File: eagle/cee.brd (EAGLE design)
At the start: 50 x 80 mm, 52 parts, among them IC1 IC1, J1 SOLDERJUMPERNC2

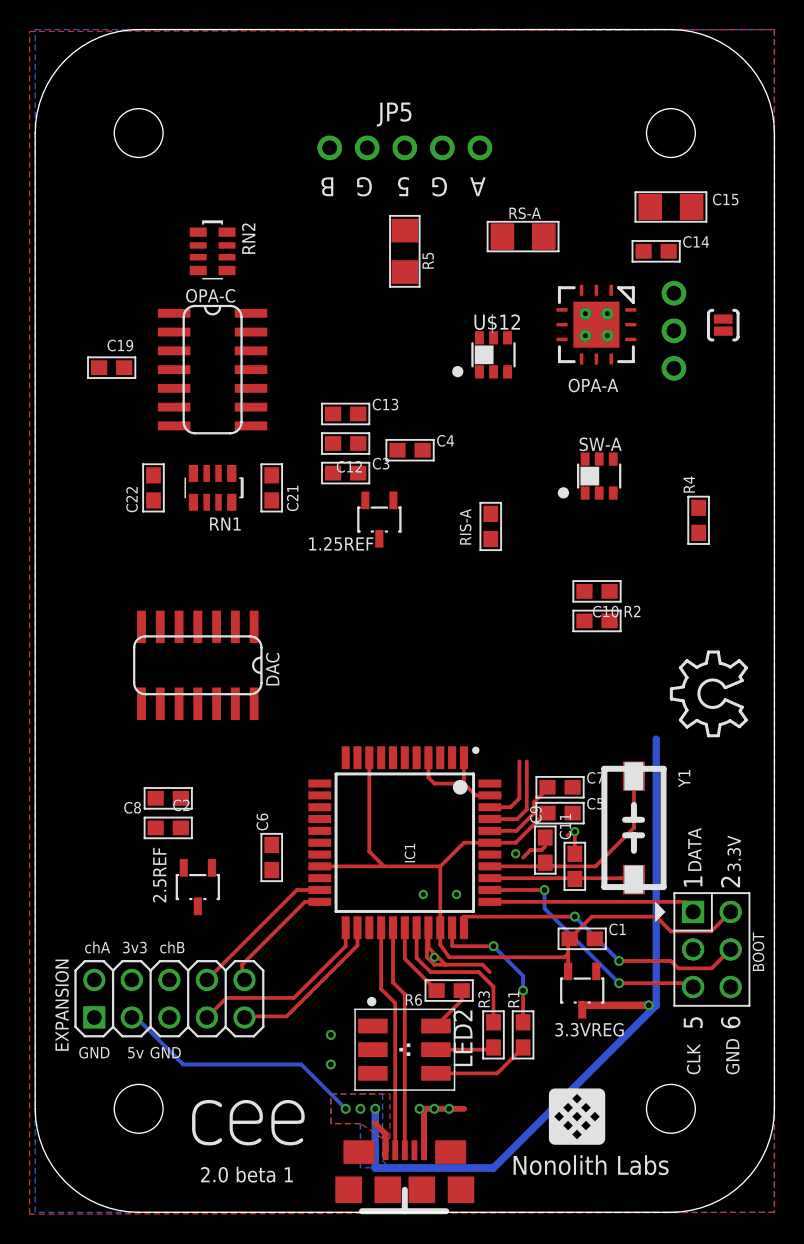
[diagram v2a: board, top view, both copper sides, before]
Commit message: more routing, moved some stuff around
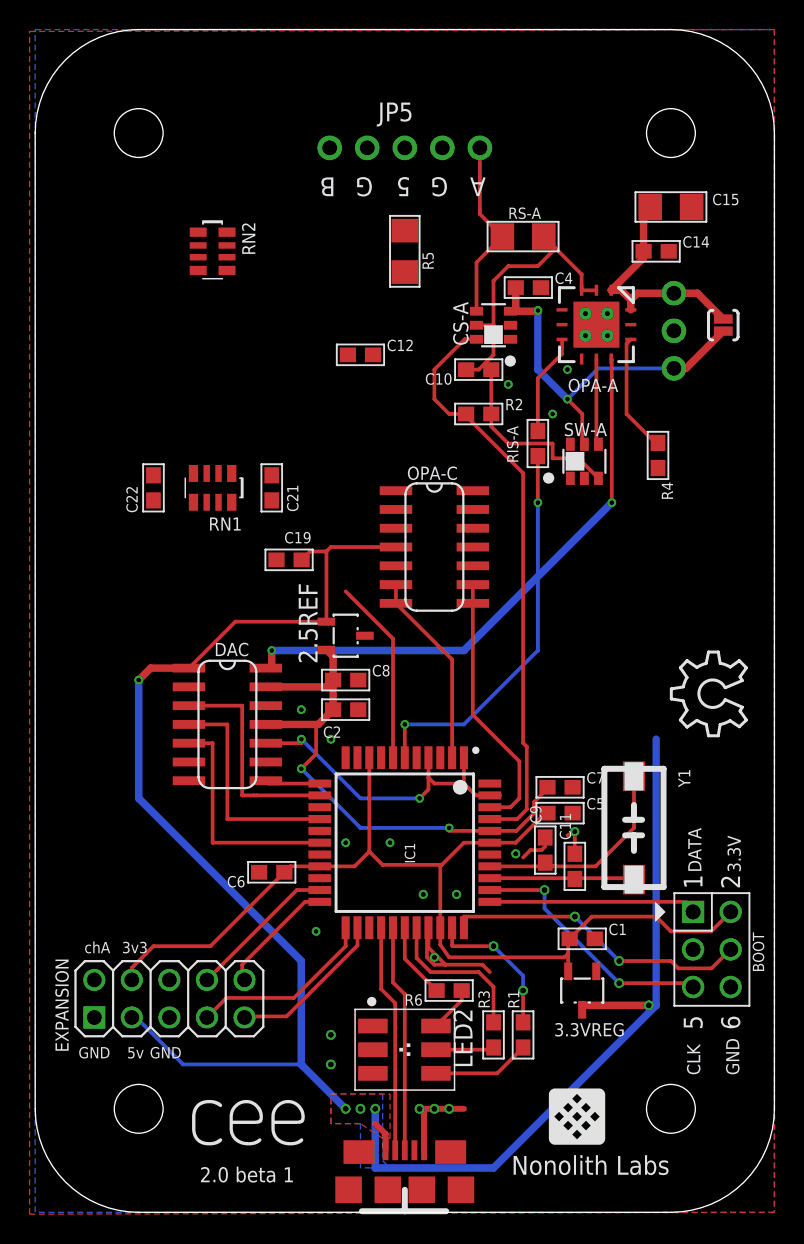
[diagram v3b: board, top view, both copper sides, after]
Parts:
- removed 1.25REF: (no value), nonolith:SOT23-3
- removed C13, C3: .01uF, nonolith:0603
- removed U$12: INA213, nonolith:SOT23-6
- added CS-A: INA213, nonolith:SOT23-6
- C12: value 1uF -> .01uF
- OPA-C: value AD86080.0254 -> AD8608
- moved 2.5REF 19.7 mm to (21.0, 39.0), turned to 90 degrees
- moved OPA-C 19.2 mm to (27.0, 45.0)
- moved C19 17.7 mm to (17.2, 44.1)
- moved C10 17.0 mm to (30.0, 57.0)
- moved R2 16.1 mm to (30.0, 54.0)
- moved C2 14.4 mm to (21.0, 34.0), turned to 0 degrees
- moved C8 14.4 mm to (21.0, 36.0), turned to 0 degrees
- moved C4 13.6 mm to (33.4, 62.5)
- moved RIS-A 6.45 mm to (34.0, 52.0)
- moved C12 6.08 mm to (22.0, 58.0)
- moved R4 5.18 mm to (42.1, 51.2), turned to 270 degrees
- moved DAC 4.47 mm to (13.0, 33.0), turned to 270 degrees
- moved SW-A 1.41 mm to (37.1, 50.8)
- moved C6 1.00 mm to (16.0, 23.0), turned to 180 degrees
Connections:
- removed net 1.25VREF: 1.25REF.2, C12.1, C13.1, C3.1, IC1.1, IC1.4, IC1.43, U$12.1
- removed net N$13: JP5.5
- removed net SMU-B: EXPANSION.6, RN2.3
- new net CSA-VREF: C12.1, CS-A.1, IC1.7
- net 5V: now also CS-A.3; no longer 1.25REF.1, U$12.3
- net GND: now also CS-A.2; no longer 1.25REF.3, C13.2, C3.2, U$12.2
- net SMU-A: now also CS-A.4; no longer U$12.4
- net VO-A: now also CS-A.5; no longer U$12.5
- net VOUT-B: now also IC1.1, IC1.4, IC1.43
- net VS-A: now also CS-A.6; no longer U$12.6
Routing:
- net 5V: track 70.0 -> 153.0 mm, vias 4 -> 7
- net VOUT-A: track 0.00 -> 38.5 mm, vias 0 -> 2
- net VS-A: track 6.02 -> 39.5 mm
- net 2.5VREF: track 5.66 -> 39.1 mm, vias 0 -> 2
- net ISET-DAC-A: track 0.00 -> 26.5 mm, vias 0 -> 2
- net VOUT-B: track 0.00 -> 22.4 mm, vias 0 -> 2
- net VO-A: track 0.00 -> 19.2 mm
- net 5V-EXT: track 0.00 -> 16.2 mm
- net 3.3V: track 53.7 -> 69.7 mm
- net MOSI: track 0.00 -> 15.6 mm
- net SCK: track 0.00 -> 15.2 mm
- net CS: track 0.00 -> 14.9 mm
- net AF-A: track 0.00 -> 13.4 mm
- net ADC-B: track 0.00 -> 13.3 mm
- net ADC-A: track 4.75 -> 18.0 mm
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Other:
- board text removed: "chB"

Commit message: did I winzorz
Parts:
- added C13: .1uF, nonolith:0603
- added C16: (no value), nonolith:0603
- added C3: 4.7uF, nonolith:0603
- added U$12: LME49726, nonolith:SO-08
- CS-A: device nonolith:SOT23-6 -> nonolith:SC-70
- moved RN2 13.9 mm to (24.0, 58.0), turned to 180 degrees
- moved C12 10.9 mm to (32.8, 56.2), turned to 270 degrees
- moved C10 1.00 mm to (29.0, 57.0), turned to 90 degrees
- moved R5 1.00 mm to (26.0, 65.0)
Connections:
- removed net 5V-EXT-P: JP5.3, R5.2
- new net 2.5VFDBK: R5.1, U$12.1
- new net 2.5VOUT: JP5.3, R5.2, U$12.2
- new net 5VOUT: JP5.5, U$12.6, U$12.7
- net 2.5VREF: now also C16.1, U$12.3
- net 5V: now also C13.1, C3.1, CS-A.P3, U$12.5, U$12.8; no longer CS-A.3
- net 5V-EXT: no longer R5.1
- net CSA-VREF: now also CS-A.P1; no longer CS-A.1
- net GND: now also C13.2, C16.2, C3.2, CS-A.P2, U$12.4; no longer CS-A.2
- net SMU-A: now also CS-A.P4; no longer CS-A.4, EXPANSION.2
- net VO-A: now also CS-A.P5; no longer CS-A.5
- net VS-A: now also CS-A.P6; no longer CS-A.6
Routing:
- net 5V: track 153.0 -> 205.3 mm, vias 7 -> 8
- net 2.5VREF: track 39.1 -> 81.6 mm, vias 2 -> 4
- net CSA-VREF: track 12.6 -> 47.0 mm, vias 0 -> 4
- net N$1: track 0.00 -> 30.1 mm, vias 0 -> 2
- net 2.5VOUT: track 0.00 -> 22.0 mm, vias 0 -> 2
- net BUFF-A: track 0.00 -> 20.7 mm, vias 0 -> 2
- net N$2: track 0.00 -> 20.3 mm, vias 0 -> 2
- net BUFF-B: track 0.00 -> 18.6 mm
- net SMUP-A: track 0.00 -> 17.0 mm
- net SMUP-SW-A: track 0.00 -> 16.1 mm, vias 0 -> 2
- net 2.5VFDBK: track 0.00 -> 14.6 mm
- net SMUP-B: track 0.00 -> 12.9 mm
- net 5VOUT: track 0.00 -> 7.56 mm
- net SMU-A: track 12.4 -> 19.3 mm
- net VS-A: track 39.5 -> 41.3 mm
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
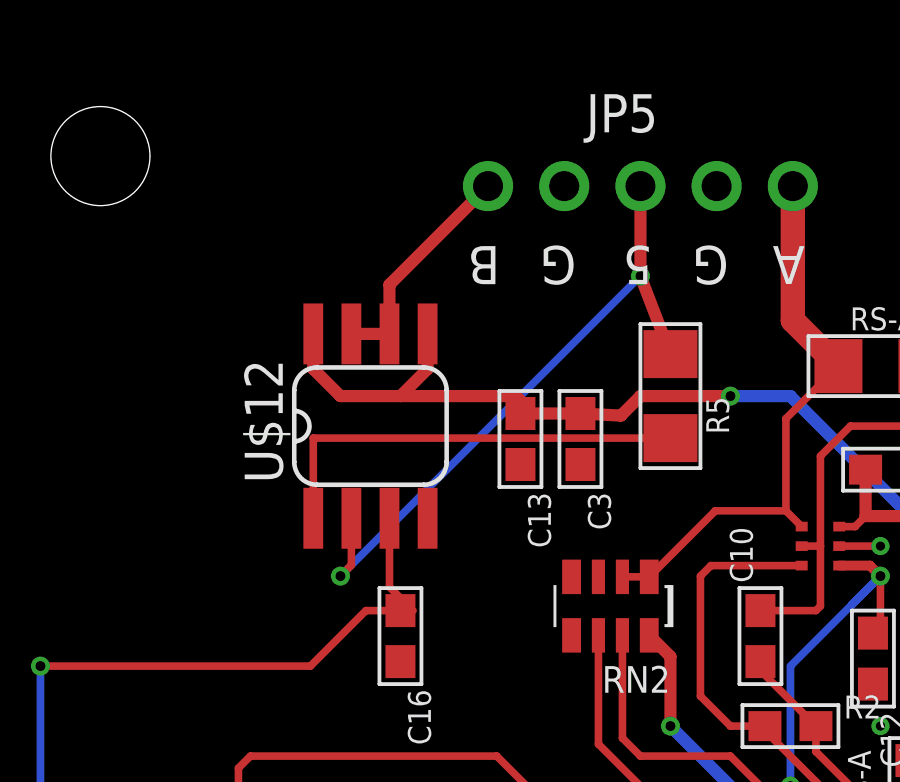
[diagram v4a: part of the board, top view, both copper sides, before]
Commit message: update package of buffer to correct layout
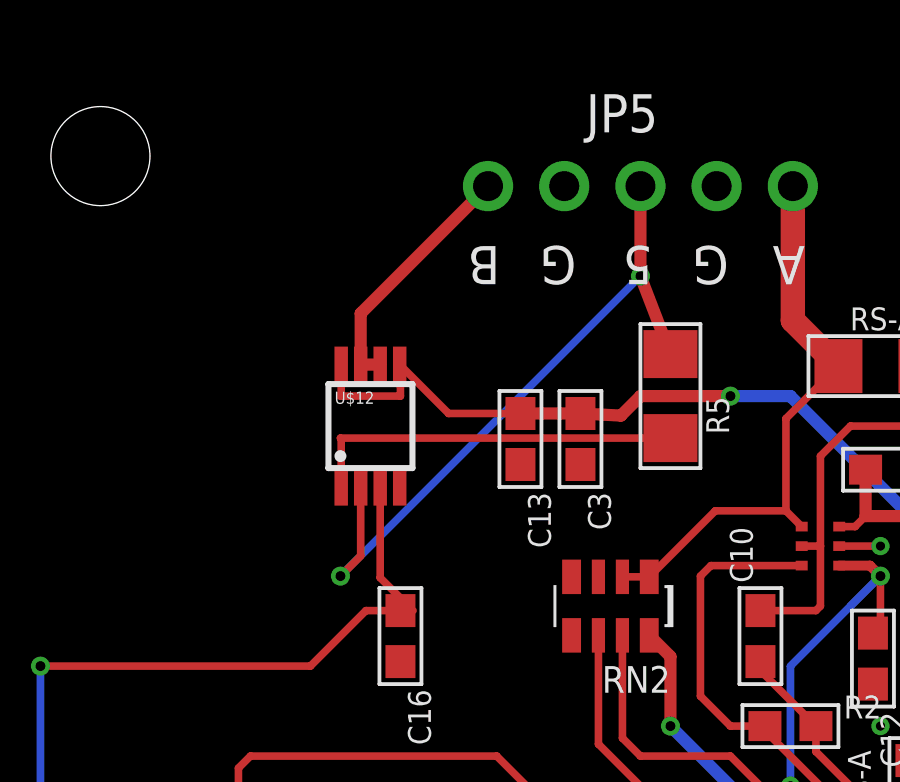
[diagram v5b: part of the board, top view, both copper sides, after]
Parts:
- U$12: device nonolith:SO-08 -> nonolith:MSOP8
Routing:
- net 5V: track 205.3 -> 202.6 mm
- net 2.5VFDBK: track 14.6 -> 12.7 mm
- net 2.5VREF: track 81.6 -> 82.8 mm
- net 2.5VOUT: track 22.0 -> 23.2 mm
- net 5VOUT: track 7.56 -> 8.36 mm
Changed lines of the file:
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@@
 <element name="CS-A" library="nonolith" package="SC-70" value="INA213" x="31" y="60" rot="R90"/>
 <element name="C12" library="nonolith" package="0603" value=".01uF" x="32.75" y="56.25" rot="R270"/>
-<element name="U$12" library="nonolith" package="SO-08" value="LME49726" x="16" y="64"/>
+<element name="U$12" library="nonolith" package="MSOP8" value="LME49726" x="16" y="64"/>
 <element name="C3" library="nonolith" package="0603" value="4.7uF" x="23" y="63.57" rot="R270"/>
 <element name="C13" library="nonolith" package="0603" value=".1uF" x="21" y="63.57" rot="R270"/>
@@
 <contactref element="C13" pad="1"/>
 <contactref element="C3" pad="1"/>
-<wire x1="18" y1="67.0734" x2="17.905" y2="67.0734" width="0.254" layer="1"/>
 <via x="28" y="65" extent="1-16" drill="0.3302"/>
 <wire x1="28" y1="65" x2="30" y2="65" width="0.4064" layer="16"/>
@@
 <wire x1="24.35" y1="64.35" x2="25" y2="65" width="0.4064" layer="1"/>
 <wire x1="25" y1="65" x2="28" y2="65" width="0.4064" layer="1"/>
-<wire x1="21" y1="64.42" x2="21" y2="64.85" width="0.4064" layer="1"/>
-<wire x1="14.095" y1="67.0734" x2="14.095" y2="65.905" width="0.4064" layer="1"/>
-<wire x1="14.095" y1="65.905" x2="15" y2="65" width="0.4064" layer="1"/>
-<wire x1="15" y1="65" x2="17" y2="65" width="0.4064" layer="1"/>
-<wire x1="17" y1="65" x2="17.905" y2="65.905" width="0.4064" layer="1"/>
-<wire x1="17.905" y1="65.905" x2="17.905" y2="67.0734" width="0.4064" layer="1"/>
-<wire x1="21" y1="64.85" x2="20.85" y2="65" width="0.4064" layer="1"/>
-<wire x1="20.85" y1="65" x2="17" y2="65" width="0.4064" layer="1"/>
+<wire x1="15.025" y1="66.05" x2="15.025" y2="65.025" width="0.254" layer="1"/>
+<wire x1="15.025" y1="65.025" x2="15" y2="65" width="0.254" layer="1"/>
+<wire x1="15" y1="65" x2="17" y2="65" width="0.254" layer="1"/>
+<wire x1="17" y1="65" x2="17" y2="66.025" width="0.254" layer="1"/>
+<wire x1="17" y1="66.025" x2="16.975" y2="66.05" width="0.254" layer="1"/>
+<wire x1="21" y1="64.42" x2="18.605" y2="64.42" width="0.254" layer="1"/>
+<wire x1="18.605" y1="64.42" x2="16.975" y2="66.05" width="0.254" layer="1"/>
 </signal>
 <signal name="GND">
@@
 <wire x1="22" y1="26" x2="28" y2="26" width="0.254" layer="16"/>
 <contactref element="U$12" pad="3"/>
-<wire x1="16.635" y1="60.9266" x2="16.635" y2="58.635" width="0.254" layer="1"/>
 <wire x1="14" y1="56" x2="5" y2="56" width="0.254" layer="1"/>
 <via x="5" y="56" extent="1-16" drill="0.3302"/>
@@
 <wire x1="14" y1="56" x2="15.85" y2="57.85" width="0.254" layer="1"/>
 <wire x1="15.85" y1="57.85" x2="17" y2="57.85" width="0.254" layer="1"/>
-<wire x1="16.635" y1="58.635" x2="17" y2="58.27" width="0.254" layer="1"/>
+<wire x1="16.325" y1="58.945" x2="17" y2="58.27" width="0.254" layer="1"/>
 <wire x1="17" y1="58.27" x2="17" y2="57.85" width="0.254" layer="1"/>
+<wire x1="16.325" y1="61.95" x2="16.325" y2="58.945" width="0.254" layer="1"/>
 <wire x1="34.75" y1="28.75" x2="34.65" y2="28.75" width="0" layer="19" extent="1-1"/>
 </signal>
@@
 <contactref element="U$12" pad="7"/>
 <contactref element="U$12" pad="6"/>
-<wire x1="16.635" y1="67.0734" x2="15.365" y2="67.0734" width="0.4064" layer="1"/>
-<wire x1="16.635" y1="67.0734" x2="16.635" y2="68.715" width="0.4064" layer="1"/>
-<wire x1="16.635" y1="68.715" x2="19.92" y2="72" width="0.4064" layer="1"/>
+<wire x1="16.325" y1="66.05" x2="15.675" y2="66.05" width="0.4064" layer="1"/>
+<wire x1="15.675" y1="67.755" x2="19.92" y2="72" width="0.4064" layer="1"/>
+<wire x1="15.675" y1="67.755" x2="15.675" y2="66.05" width="0.4064" layer="1"/>
 </signal>
 <signal name="2.5VOUT">
@@
 <wire x1="25" y1="69" x2="26" y2="66.4" width="0.4064" layer="1"/>
 <wire x1="25" y1="72" x2="25" y2="69" width="0.4064" layer="1"/>
-<wire x1="15.365" y1="60.9266" x2="15.365" y2="59.365" width="0.254" layer="1"/>
-<wire x1="15.365" y1="59.365" x2="15" y2="59" width="0.254" layer="1"/>
+<wire x1="15.675" y1="59.675" x2="15" y2="59" width="0.254" layer="1"/>
 <via x="15" y="59" extent="1-16" drill="0.3302"/>
 <wire x1="15" y1="59" x2="25" y2="69" width="0.254" layer="16"/>
+<wire x1="15.675" y1="59.675" x2="15.675" y2="61.95" width="0.254" layer="1"/>
 </signal>
 <signal name="2.5VFDBK">
 <contactref element="U$12" pad="1"/>
 <contactref element="R5" pad="1"/>
-<wire x1="14.095" y1="63.6" x2="26" y2="63.6" width="0.254" layer="1"/>
-<wire x1="14.095" y1="63.6" x2="14.095" y2="60.9266" width="0.254" layer="1"/>
+<wire x1="15" y1="63.6" x2="26" y2="63.6" width="0.254" layer="1"/>
+<wire x1="15.025" y1="61.95" x2="15.025" y2="63.575" width="0.254" layer="1"/>
+<wire x1="15.025" y1="63.575" x2="15" y2="63.6" width="0.254" layer="1"/>
 </signal>
 </signals>

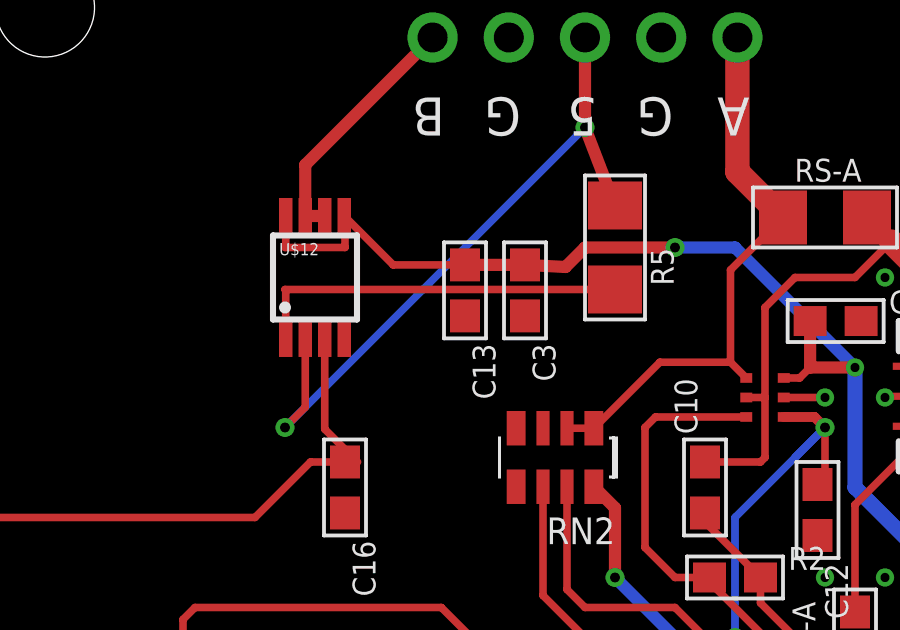
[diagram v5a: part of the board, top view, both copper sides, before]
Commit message: fix drc error - tolerance on trace running under resistors
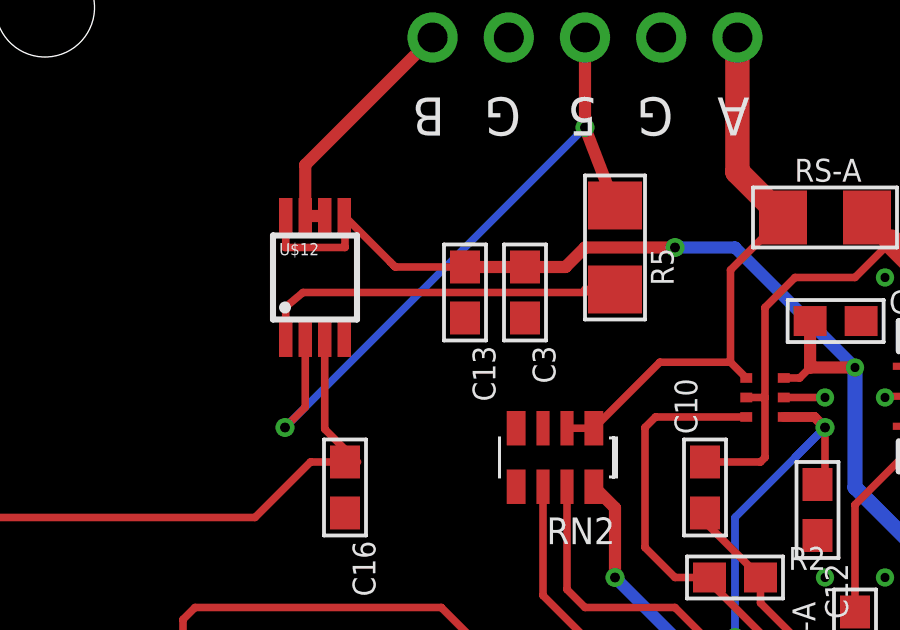
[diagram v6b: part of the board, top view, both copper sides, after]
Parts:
- moved C13 0.07 mm to (21.0, 63.5)
- moved C3 0.07 mm to (23.0, 63.5)
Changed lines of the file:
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@@
 <element name="C12" library="nonolith" package="0603" value=".01uF" x="32.75" y="56.25" rot="R270"/>
 <element name="U$12" library="nonolith" package="MSOP8" value="LME49726" x="16" y="64"/>
-<element name="C3" library="nonolith" package="0603" value="4.7uF" x="23" y="63.57" rot="R270"/>
-<element name="C13" library="nonolith" package="0603" value=".1uF" x="21" y="63.57" rot="R270"/>
+<element name="C3" library="nonolith" package="0603" value="4.7uF" x="23" y="63.5" rot="R270"/>
+<element name="C13" library="nonolith" package="0603" value=".1uF" x="21" y="63.5" rot="R270"/>
 <element name="C16" library="nonolith" package="0603" value="" x="17" y="57" rot="R270"/>
 </elements>
@@
 <wire x1="42" y1="32" x2="42" y2="55.8798" width="0.6096" layer="16"/>
 <wire x1="42" y1="55.8798" x2="43.2052" y2="57.085" width="0.6096" layer="16"/>
-<wire x1="21" y1="64.42" x2="23" y2="64.42" width="0.4064" layer="1"/>
-<wire x1="23" y1="64.42" x2="24.35" y2="64.35" width="0.4064" layer="1"/>
+<wire x1="21" y1="64.35" x2="23" y2="64.35" width="0.4064" layer="1"/>
+<wire x1="23" y1="64.35" x2="24.35" y2="64.35" width="0.4064" layer="1"/>
 <wire x1="24.35" y1="64.35" x2="25" y2="65" width="0.4064" layer="1"/>
 <wire x1="25" y1="65" x2="28" y2="65" width="0.4064" layer="1"/>
@@
 <wire x1="17" y1="65" x2="17" y2="66.025" width="0.254" layer="1"/>
 <wire x1="17" y1="66.025" x2="16.975" y2="66.05" width="0.254" layer="1"/>
-<wire x1="21" y1="64.42" x2="18.605" y2="64.42" width="0.254" layer="1"/>
-<wire x1="18.605" y1="64.42" x2="16.975" y2="66.05" width="0.254" layer="1"/>
+<wire x1="18.605" y1="64.42" x2="18.5125" y2="64.5125" width="0.254" layer="1"/>
+<wire x1="18.5125" y1="64.5125" x2="16.975" y2="66.05" width="0.254" layer="1"/>
+<wire x1="21" y1="64.35" x2="18.675" y2="64.35" width="0.254" layer="1"/>
+<wire x1="18.675" y1="64.35" x2="18.605" y2="64.42" width="0.254" layer="1"/>
 </signal>
 <signal name="GND">
@@
 <contactref element="U$12" pad="1"/>
 <contactref element="R5" pad="1"/>
-<wire x1="15" y1="63.6" x2="26" y2="63.6" width="0.254" layer="1"/>
-<wire x1="15.025" y1="61.95" x2="15.025" y2="63.575" width="0.254" layer="1"/>
-<wire x1="15.025" y1="63.575" x2="15" y2="63.6" width="0.254" layer="1"/>
+<wire x1="15.025" y1="61.95" x2="15.025" y2="62.975" width="0.254" layer="1"/>
+<wire x1="15.025" y1="62.975" x2="15" y2="63" width="0.254" layer="1"/>
+<wire x1="15" y1="63" x2="15.6" y2="63.5" width="0.254" layer="1"/>
+<wire x1="15.6" y1="63.5" x2="25" y2="63.5" width="0.254" layer="1"/>
+<wire x1="25" y1="63.5" x2="25" y2="63.6" width="0.254" layer="1"/>
+<wire x1="25" y1="63.6" x2="26" y2="63.6" width="0.254" layer="1"/>
 </signal>
 </signals>
